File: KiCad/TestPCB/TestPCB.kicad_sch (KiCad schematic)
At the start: 73 parts, among them U1 MC33078, U2 TLC274, U3 MC33078, U4 MC33078, U5 MC33078, U6 TLC274, U7 REF192, U8 DAC5578xPW

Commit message: Schematic re-accommodating
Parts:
- removed JP2, JP3, JP4, JP5, JP6, JP7: Jumper_2_Bridged, symbol Jumper:Jumper_2_Bridged
- removed R12, R13, R14, R15, R16, R17, R2, R3, R4, R5, R6, R7: 10k, symbol Device:R
- removed R22, R23, R24, R25, R26, R27: 1meg, symbol Device:R
- removed R32, R33, R34, R35, R36, R37: 10, symbol Device:R
- removed TP0, TP1, TP2, TP3, TP4, TP5, TP6, TP7: TestPoint, symbol Connector:TestPoint
- removed unit 3 of U2
- removed unit 4 of U2
- removed U5: MC33078, symbol Amplifier_Operational:MC33078
- added JPout_U2a, JPout_U2b, JPout_U3a, JPout_U3b, JPout_U4a, JPout_U4b: Jumper_2_Bridged, symbol Jumper:Jumper_2_Bridged
- added Rain_U5c, Rain_U5d, Rain_U6a, Rain_U6b, Rain_U6c, Rain_U6d: 1meg, symbol Device:R
- added Rbin_U5c, Rbin_U5d, Rbin_U6a, Rbin_U6b, Rbin_U6c, Rbin_U6d: 10, symbol Device:R
- added Rf_U2a, Rf_U2b, Rf_U3a, Rf_U3b, Rf_U4a, Rf_U4b, Rin-_U2a, Rin-_U2b, Rin-_U3a, Rin-_U3b, Rin-_U4a, Rin-_U4b: 10k, symbol Device:R
- added unit 2 of U2
- added unit 1 of U2
- added unit 4 of U5
- added unit 3 of U5
- U3, U4: value MC33078 -> (none)
- U5: renamed from U2; value TLC274 -> (none)
- U6: value TLC274 -> (none)
- gave numbers to parts that had none: 6
- renumbered JP0 to JPout_U1a, JP1 to JPout_U1b, R20 to Rain_U5a, R21 to Rain_U5b, R30 to Rbin_U5a, R31 to Rbin_U5b, R10 to Rf_U1a, R11 to Rf_U1b, R0 to Rin-_U1a, R1 to Rin-_U1b
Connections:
- net GND: now also U8.14 (GND), Rbin_U5c.2, Rbin_U5d.2, Rbin_U6a.2, Rbin_U6b.2, Rbin_U6c.2, Rbin_U6d.2
- net -2V5: now reaches U1.4 (V-)
- net -2V5: now also U2.4 (V-), U3.4 (V-), U4.4 (V-), U5.11 (V-), U6.11 (V-)
- net at U3.1: now also JPout_U3a.1 (A), Rf_U3a.2
- net at U3.2 (-): now also Rf_U3a.1, Rin-_U3a.2
- net at U8.5 (VOUTC): now also U2.3 (+); no longer U3.3 (+)
- net at U3.5 (+): now also U8.11 (VOUTF); no longer U8.12 (VOUTD)
- net at U3.6 (-): now also Rf_U3b.1, Rin-_U3b.2
- net at U3.7: now also JPout_U3b.1 (A), Rf_U3b.2
- net at U4.5 (+): now also U8.10 (VOUTH); no longer U8.11 (VOUTF)
- net at U4.6 (-): now also Rf_U4b.1, Rin-_U4b.2
- net at U4.7: now also JPout_U4b.1 (A), Rf_U4b.2
- net at U4.1: now also JPout_U4a.1 (A), Rf_U4a.2
- net at U4.2 (-): now also Rf_U4a.1, Rin-_U4a.2
- net at U8.6 (VOUTE): now also U3.3 (+); no longer U4.3 (+)
- net at U8.7 (VOUTG): now also U4.3 (+)
- net at U6.3 (+): now also Rain_U6a.2, Rbin_U6a.1
- net at U6.10 (+): now also Rain_U6c.2, Rbin_U6c.1
- net at U6.12 (+): now also Rain_U6d.2, Rbin_U6d.1
- net at U6.5 (+): now also Rain_U6b.2, Rbin_U6b.1
- net at C3.1, Rin-_U1a.1, Rin-_U1b.1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: now also Rin-_U2a.1, Rin-_U2b.1, Rin-_U3a.1, Rin-_U3b.1, Rin-_U4a.1, Rin-_U4b.1
- new net: U2.5 (+), U8.12 (VOUTD)
- new net: Rf_U2b.1, Rin-_U2b.2, U2.6 (-)
- new net: JPout_U2b.1 (A), Rf_U2b.2, U2.7
- new net: JPout_U2a.1 (A), Rf_U2a.2, U2.1
- new net: JPout_U2a.2 (B), Rain_U5c.1
- new net: JPout_U4a.2 (B), Rain_U6c.1
- new net: JPout_U3b.2 (B), Rain_U6b.1
- new net: JPout_U4b.2 (B), Rain_U6d.1
- new net: Rf_U2a.1, Rin-_U2a.2, U2.2 (-)
- new net: JPout_U2b.2 (B), Rain_U5d.1
- new net: Rain_U5d.2, Rbin_U5d.1, U5.12 (+)
- new net: U5.13 (-), U5.14
- new net: Rain_U5c.2, Rbin_U5c.1, U5.10 (+)
- new net: U5.8, U5.9 (-)
- new net: JPout_U3a.2 (B), Rain_U6a.1
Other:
- moved on the sheet: C1, C2, C3, JPout_U1a, JPout_U1b, J_LDAC, J_SCL, J_SDA, J_SYNC, R_SCL, R_SDA, Rain_U5a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

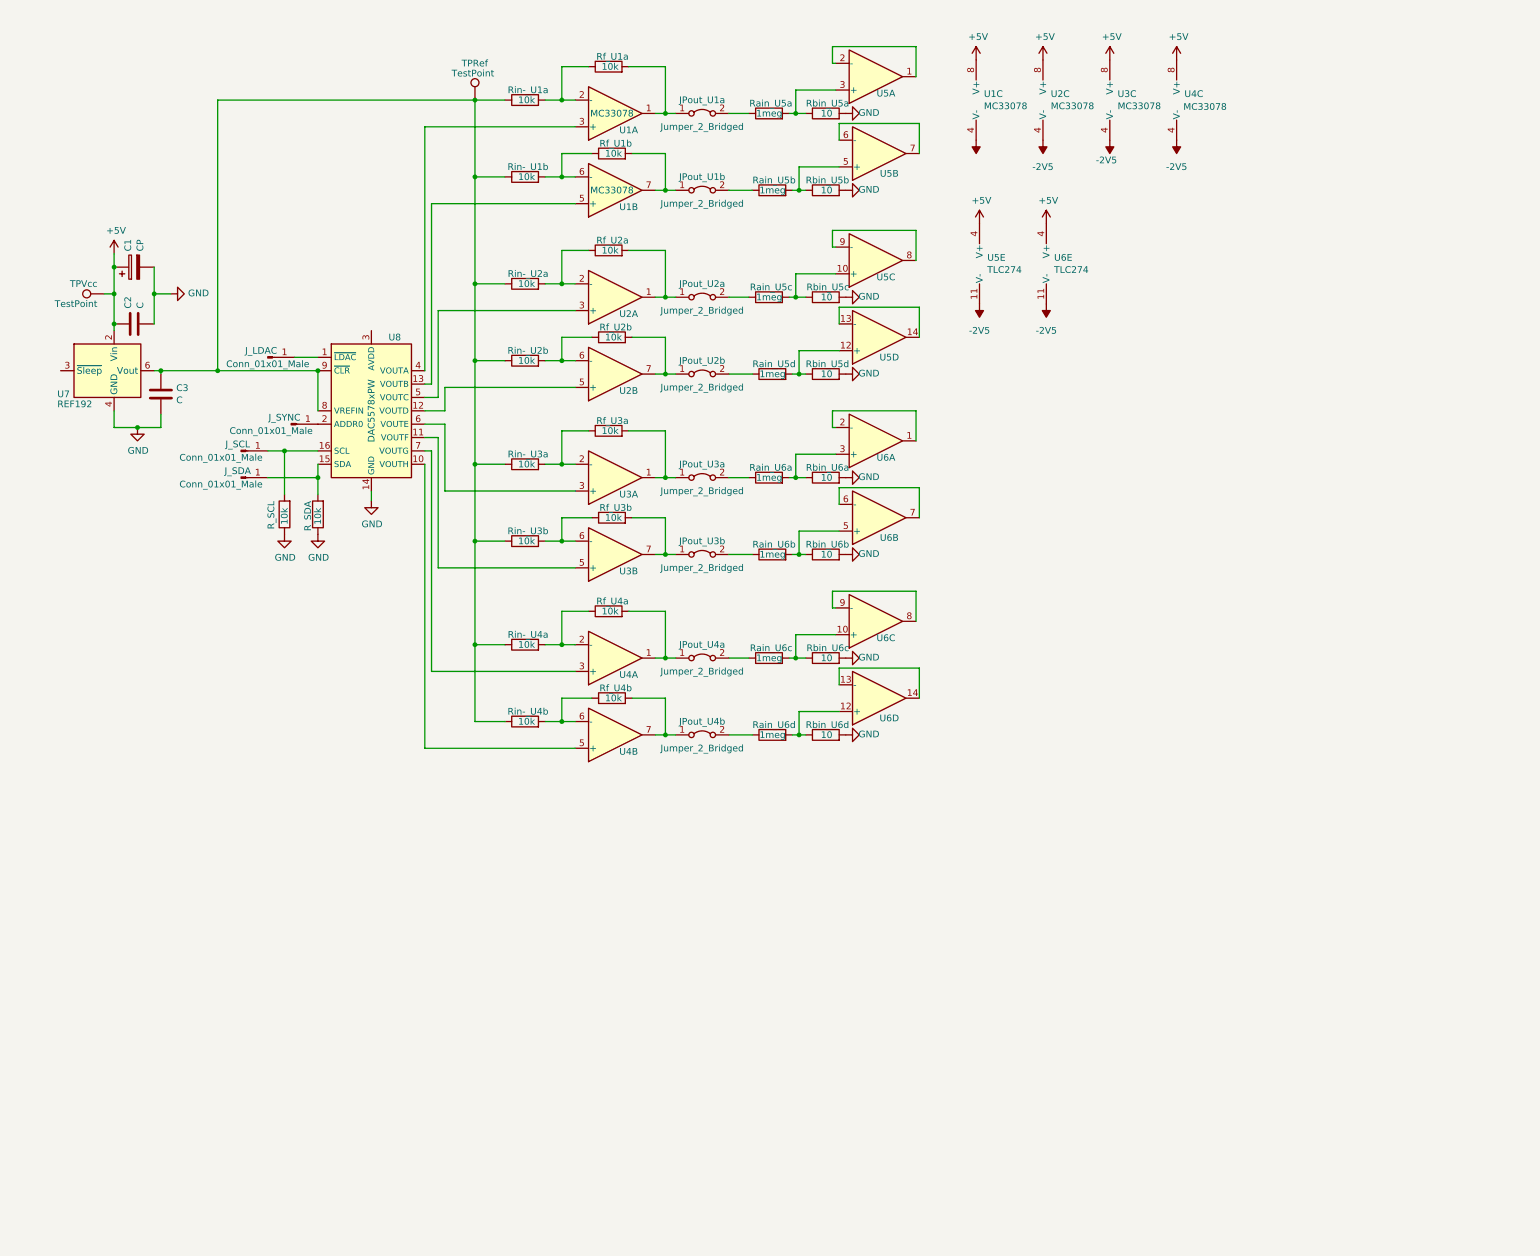
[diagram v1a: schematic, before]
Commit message: component naming and some footprints
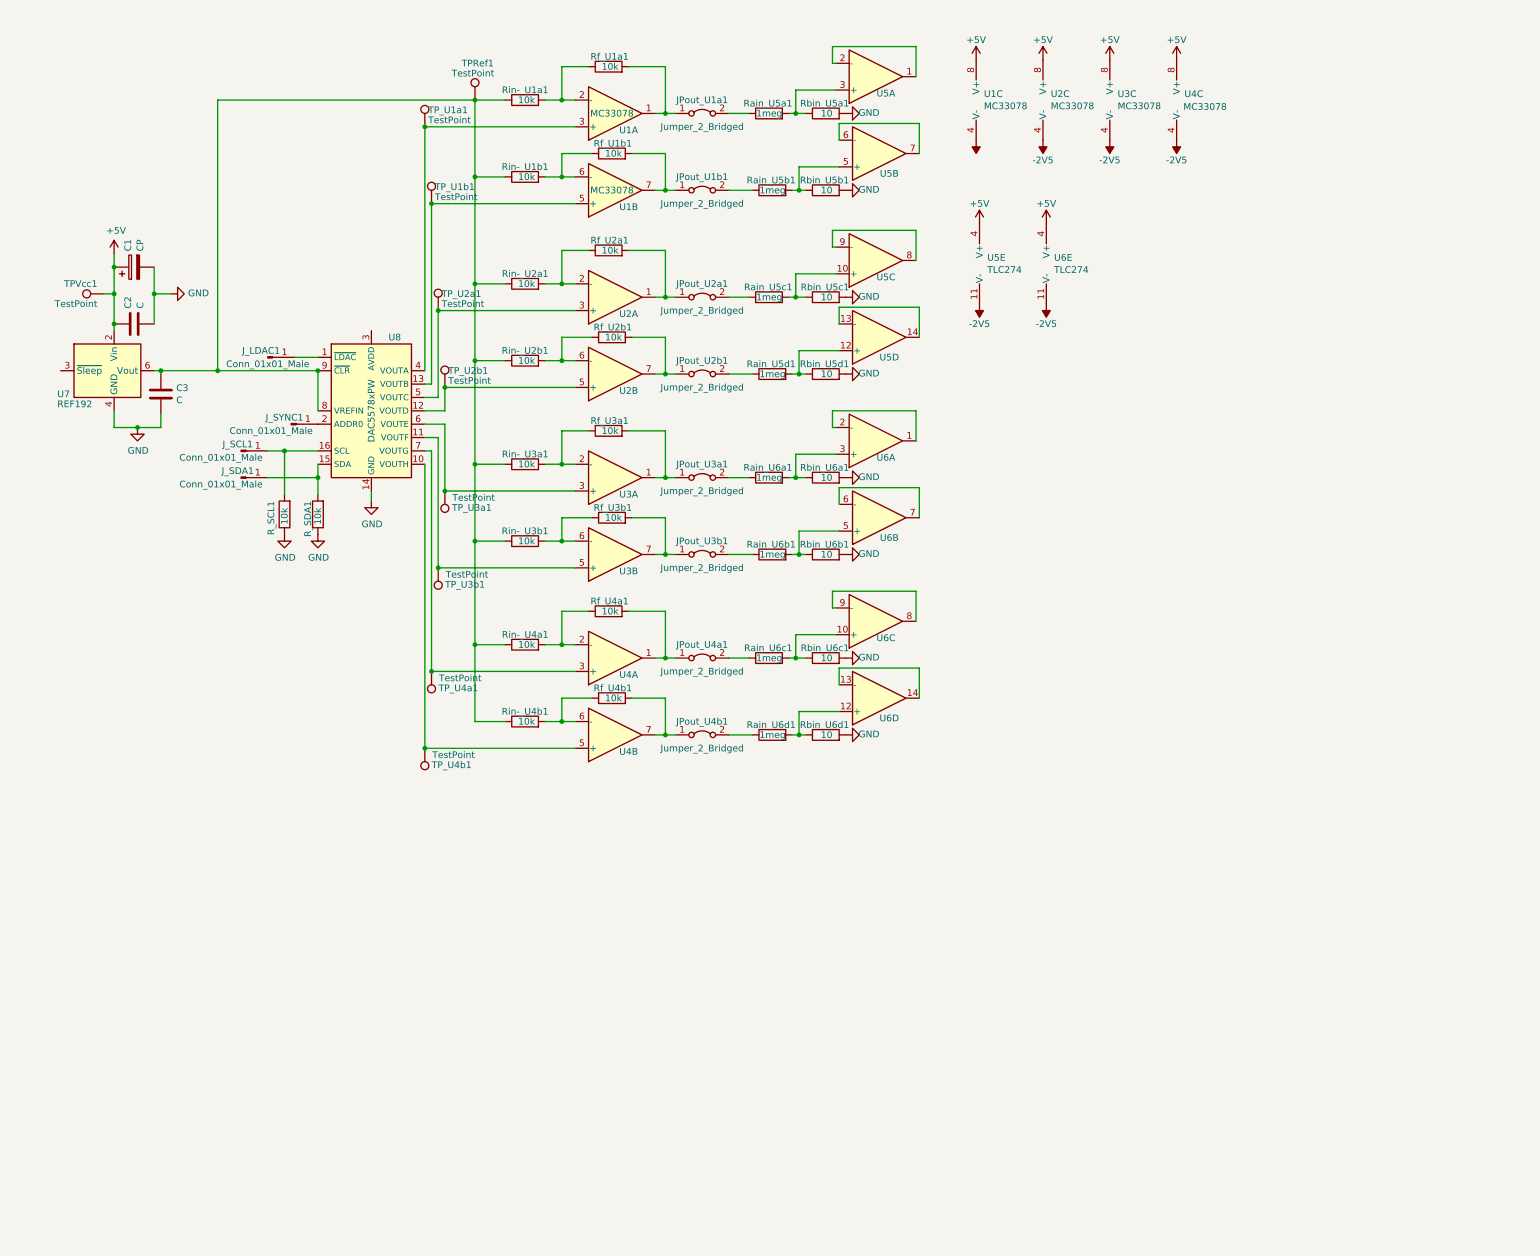
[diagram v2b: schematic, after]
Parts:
- added TP_U1a1, TP_U1b1, TP_U2a1, TP_U2b1, TP_U3a1, TP_U3b1, TP_U4a1, TP_U4b1: TestPoint, symbol Connector:TestPoint
- renumbered JPout_U1a to JPout_U1a1, JPout_U1b to JPout_U1b1, JPout_U2a to JPout_U2a1, JPout_U2b to JPout_U2b1, JPout_U3a to JPout_U3a1, JPout_U3b to JPout_U3b1, JPout_U4a to JPout_U4a1, JPout_U4b to JPout_U4b1, J_LDAC to J_LDAC1, J_SCL to J_SCL1, J_SDA to J_SDA1, J_SYNC to J_SYNC1, R_SCL to R_SCL1, R_SDA to R_SDA1, Rain_U5a to Rain_U5a1, Rain_U5b to Rain_U5b1, Rain_U5c to Rain_U5c1, Rain_U5d to Rain_U5d1, Rain_U6a to Rain_U6a1, Rain_U6b to Rain_U6b1, Rain_U6c to Rain_U6c1, Rain_U6d to Rain_U6d1, Rbin_U5a to Rbin_U5a1, Rbin_U5b to Rbin_U5b1, Rbin_U5c to Rbin_U5c1, Rbin_U5d to Rbin_U5d1, Rbin_U6a to Rbin_U6a1, Rbin_U6b to Rbin_U6b1, Rbin_U6c to Rbin_U6c1, Rbin_U6d to Rbin_U6d1, Rf_U1a to Rf_U1a1, Rf_U1b to Rf_U1b1, Rf_U2a to Rf_U2a1, Rf_U2b to Rf_U2b1, Rf_U3a to Rf_U3a1, Rf_U3b to Rf_U3b1, Rf_U4a to Rf_U4a1, Rf_U4b to Rf_U4b1, Rin-_U1a to Rin-_U1a1, Rin-_U1b to Rin-_U1b1, Rin-_U2a to Rin-_U2a1, Rin-_U2b to Rin-_U2b1, Rin-_U3a to Rin-_U3a1, Rin-_U3b to Rin-_U3b1, Rin-_U4a to Rin-_U4a1, Rin-_U4b to Rin-_U4b1, TPRef to TPRef1, TPVcc to TPVcc1
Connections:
- net at U1.3 (+), U8.4 (VOUTA): now also TP_U1a1.1
- net at U1.5 (+), U8.13 (VOUTB): now also TP_U1b1.1
- net at U4.5 (+), U8.10 (VOUTH): now also TP_U4b1.1
- net at U3.5 (+), U8.11 (VOUTF): now also TP_U3b1.1
- net at U2.5 (+), U8.12 (VOUTD): now also TP_U2b1.1
- net at U2.3 (+), U8.5 (VOUTC): now also TP_U2a1.1
- net at U3.3 (+), U8.6 (VOUTE): now also TP_U3a1.1
- net at U4.3 (+), U8.7 (VOUTG): now also TP_U4a1.1

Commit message: schematic done, mock footprints assigned
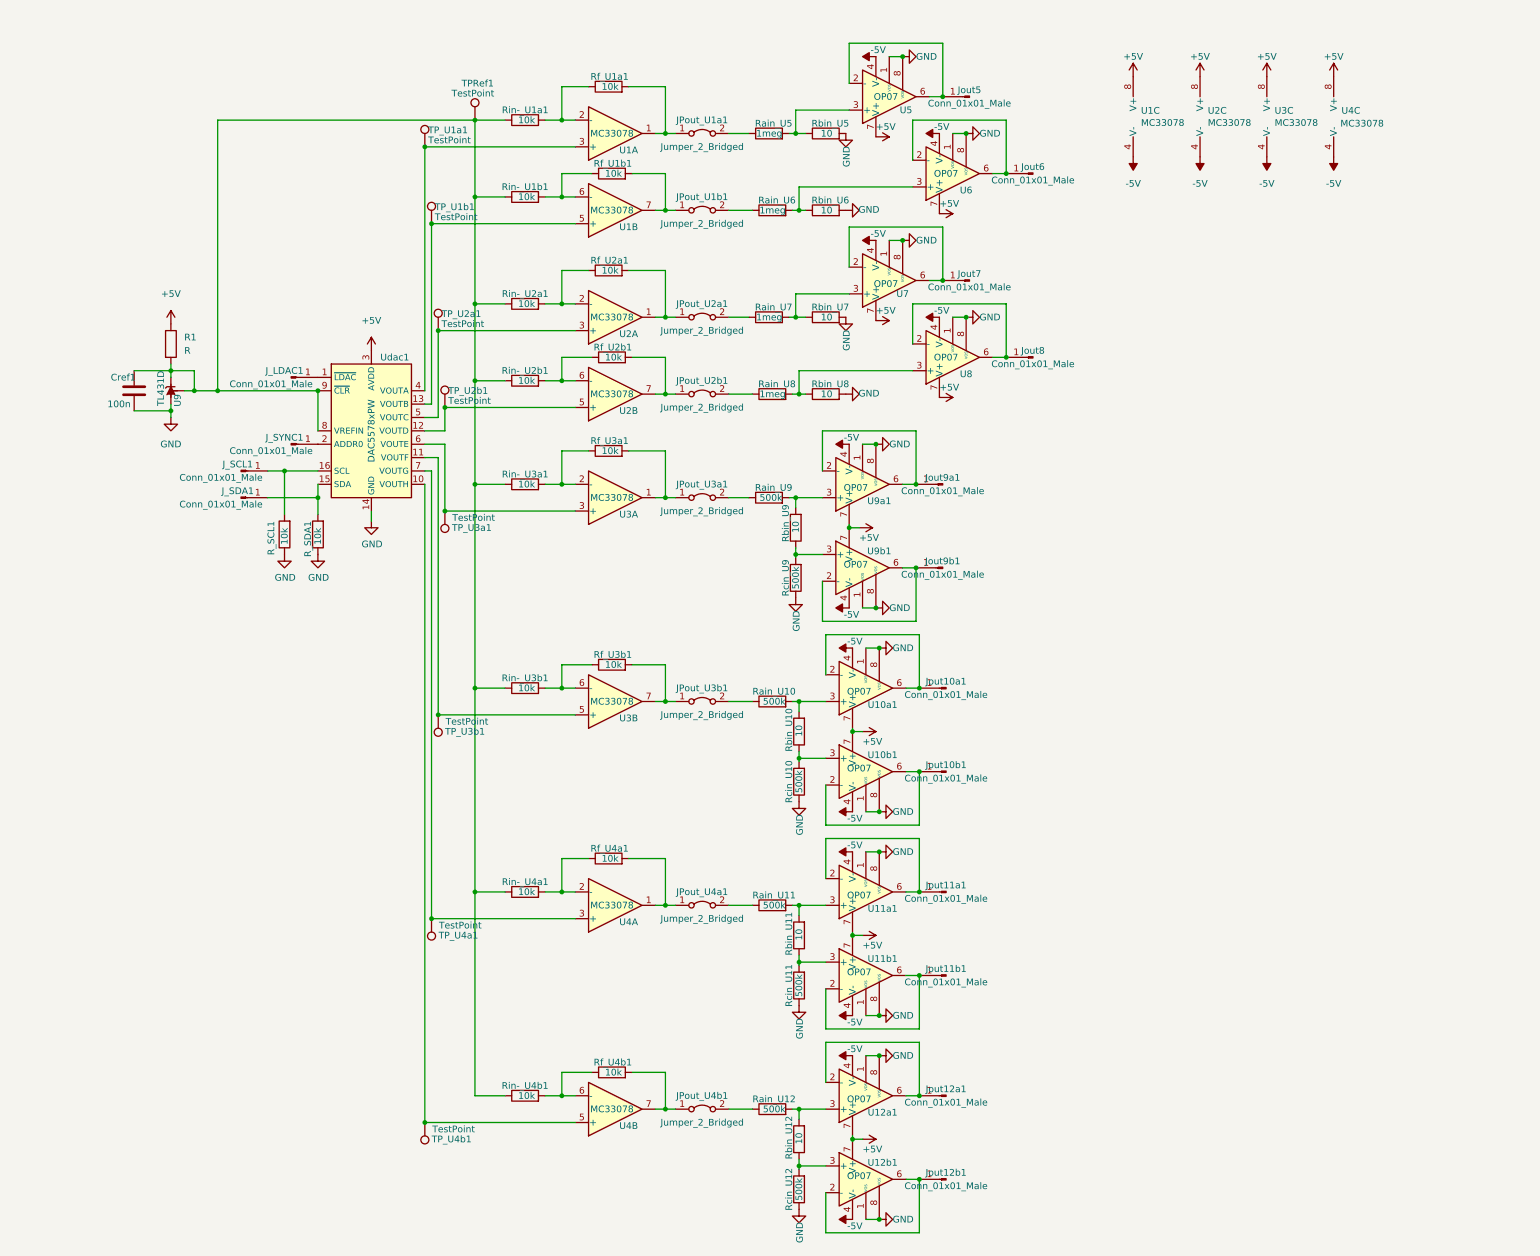
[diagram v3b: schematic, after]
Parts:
- removed C1: CP, symbol TestPCB-rescue:CP-Device
- removed C2, C3: C, symbol Device:C
- removed Rain_U6b1, Rain_U6c1, Rain_U6d1: 1meg, symbol Device:R
- removed Rbin_U6b1, Rbin_U6c1, Rbin_U6d1: 10, symbol Device:R
- removed TPVcc1: TestPoint, symbol Connector:TestPoint
- removed U5: (no value), symbol Amplifier_Operational:TLC274
- removed U6: TLC274, symbol Amplifier_Operational:TLC274
- removed U7: REF192, symbol Reference_Voltage:REF192
- added Cref1: 100n, Capacitor_THT:C_Disc_D5.0mm_W2.5mm_P5.00mm, symbol Device:C
- added Jout10a1, Jout10b1, Jout11a1, Jout11b1, Jout12a1, Jout12b1, Jout5, Jout6, Jout7, Jout8, Jout9a1, Jout9b1: Conn_01x01_Male, Connector_PinHeader_2.54mm:PinHeader_1x01_P2.54mm_Vertical, symbol Connector:Conn_01x01_Male
- added R1: R, Resistor_THT:R_Axial_DIN0207_L6.3mm_D2.5mm_P10.16mm_Horizontal, symbol Device:R
- added Rain_U10, Rain_U11, Rain_U12, Rcin_U10, Rcin_U11, Rcin_U12, Rcin_U9: 500k, Resistor_SMD:R_2010_5025Metric_Pad1.40x2.65mm_HandSolder, symbol Device:R
- added Rbin_U10, Rbin_U11, Rbin_U12: 10, Resistor_SMD:R_2010_5025Metric_Pad1.40x2.65mm_HandSolder, symbol Device:R
- added U10a1, U10b1, U11a1, U11b1, U12a1, U12b1, U5, U6, U7, U8, U9a1, U9b1: OP07, Package_SO:SOIC-8_3.9x4.9mm_P1.27mm, symbol Amplifier_Operational:OP07
- added U9: TL431D, Package_SO:SOIC-8_3.9x4.9mm_P1.27mm, symbol Reference_Voltage:TL431D
- JPout_U1a1, JPout_U1b1, JPout_U2a1, JPout_U2b1, JPout_U3a1, JPout_U3b1, JPout_U4a1, JPout_U4b1: footprint (none) -> Connector_PinHeader_2.54mm:PinHeader_1x02_P2.54mm_Vertical
- J_LDAC1, J_SCL1, J_SDA1, J_SYNC1: footprint (none) -> Connector_PinHeader_2.54mm:PinHeader_1x01_P2.54mm_Vertical
- R_SCL1, R_SDA1, Rf_U1a1, Rf_U1b1, Rf_U2a1, Rf_U2b1, Rf_U3a1, Rf_U3b1, Rf_U4a1, Rf_U4b1, Rin-_U1a1, Rin-_U1b1, Rin-_U2a1, Rin-_U2b1, Rin-_U3a1, Rin-_U3b1, Rin-_U4a1, Rin-_U4b1: footprint (none) -> Resistor_THT:R_Axial_DIN0207_L6.3mm_D2.5mm_P10.16mm_Horizontal
- Rain_U5: renamed from Rain_U5a1; footprint (none) -> Resistor_SMD:R_2010_5025Metric_Pad1.40x2.65mm_HandSolder
- Rain_U6: renamed from Rain_U5b1; footprint (none) -> Resistor_SMD:R_2010_5025Metric_Pad1.40x2.65mm_HandSolder
- Rain_U7: renamed from Rain_U5c1; footprint (none) -> Resistor_SMD:R_2010_5025Metric_Pad1.40x2.65mm_HandSolder
- Rain_U8: renamed from Rain_U5d1; footprint (none) -> Resistor_SMD:R_2010_5025Metric_Pad1.40x2.65mm_HandSolder
- Rain_U9: renamed from Rain_U6a1; value 1meg -> 500k; footprint (none) -> Resistor_SMD:R_2010_5025Metric_Pad1.40x2.65mm_HandSolder
- Rbin_U5: renamed from Rbin_U5a1; footprint (none) -> Resistor_SMD:R_2010_5025Metric_Pad1.40x2.65mm_HandSolder
- Rbin_U6: renamed from Rbin_U5b1; footprint (none) -> Resistor_SMD:R_2010_5025Metric_Pad1.40x2.65mm_HandSolder
- Rbin_U7: renamed from Rbin_U5c1; footprint (none) -> Resistor_SMD:R_2010_5025Metric_Pad1.40x2.65mm_HandSolder
- Rbin_U8: renamed from Rbin_U5d1; footprint (none) -> Resistor_SMD:R_2010_5025Metric_Pad1.40x2.65mm_HandSolder
- Rbin_U9: renamed from Rbin_U6a1; footprint (none) -> Resistor_SMD:R_2010_5025Metric_Pad1.40x2.65mm_HandSolder
- TPRef1, TP_U1a1, TP_U1b1, TP_U2a1, TP_U2b1, TP_U3a1, TP_U3b1, TP_U4a1, TP_U4b1: footprint (none) -> TestPoint:TestPoint_Pad_4.0x4.0mm
- U1, U2, U3, U4: footprint (none) -> Package_DIP:DIP-8_W7.62mm_Socket_LongPads
- U2, U3, U4: value (none) -> MC33078; footprint (none) -> Package_DIP:DIP-8_W7.62mm_Socket_LongPads
- renumbered U8 to Udac1
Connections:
- net +5V: now also Udac1.3 (AVDD), R1.1, U10a1.7 (V+), U10b1.7 (V+), U11a1.7 (V+), U11b1.7 (V+), U12a1.7 (V+), U12b1.7 (V+), U5.7 (V+), U6.7 (V+), U7.7 (V+), U8.7 (V+), U9a1.7 (V+), U9b1.7 (V+)
- net GND: now also Cref1.2, Rcin_U10.1, Rcin_U11.1, Rcin_U12.1, Rcin_U9.1, U10a1.1 (VOS), U10a1.8 (VOS), U10b1.1 (VOS), U10b1.8 (VOS), U11a1.1 (VOS), U11a1.8 (VOS), U11b1.1 (VOS), U11b1.8 (VOS), U12a1.1 (VOS), U12a1.8 (VOS), U12b1.1 (VOS), U12b1.8 (VOS), U5.1 (VOS), U5.8 (VOS), U6.1 (VOS), U6.8 (VOS), U7.1 (VOS), U7.8 (VOS), U8.1 (VOS), U8.8 (VOS), U9.2 (A), U9.3 (A), U9.6 (A), U9.7 (A), U9a1.1 (VOS), U9a1.8 (VOS), U9b1.1 (VOS), U9b1.8 (VOS); no longer Rbin_U9.2
- net at Rain_U5.2, Rbin_U5.1: now also U5.3 (+)
- net at Rain_U6.2, Rbin_U6.1: now also U6.3 (+)
- net at Rin-_U1a1.1, Rin-_U1b1.1, Rin-_U2a1.1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: now also Cref1.1, R1.2, U9.1 (K), U9.8 (REF)
- net at JPout_U4a1.2 (B): now also Rain_U11.1
- net at JPout_U3b1.2 (B): now also Rain_U10.1
- net at JPout_U4b1.2 (B): now also Rain_U12.1
- net at Rbin_U9.1: now also Rcin_U9.2, U9b1.3 (+); no longer Rain_U9.2
- net at Rain_U8.2, Rbin_U8.1: now also U8.3 (+)
- net at Rain_U7.2, Rbin_U7.1: now also U7.3 (+)
- net -2V5 renamed -5V
- net -5V: now also U10a1.4 (V-), U10b1.4 (V-), U11a1.4 (V-), U11b1.4 (V-), U12a1.4 (V-), U12b1.4 (V-), U5.4 (V-), U6.4 (V-), U7.4 (V-), U8.4 (V-), U9a1.4 (V-), U9b1.4 (V-)
- new net: Jout8.1 (Pin_1), U8.2 (-), U8.6
- new net: Jout10a1.1 (Pin_1), U10a1.2 (-), U10a1.6
- new net: Rain_U10.2, Rbin_U10.2, U10a1.3 (+)
- new net: Jout9a1.1 (Pin_1), U9a1.2 (-), U9a1.6
- new net: Jout9b1.1 (Pin_1), U9b1.2 (-), U9b1.6
- new net: Jout11a1.1 (Pin_1), U11a1.2 (-), U11a1.6
- new net: Jout10b1.1 (Pin_1), U10b1.2 (-), U10b1.6
- new net: Jout6.1 (Pin_1), U6.2 (-), U6.6
- new net: Rbin_U10.1, Rcin_U10.2, U10b1.3 (+)
- new net: Jout12b1.1 (Pin_1), U12b1.2 (-), U12b1.6
- new net: Rbin_U11.1, Rcin_U11.2, U11b1.3 (+)
- new net: Rain_U9.2, Rbin_U9.2, U9a1.3 (+)
- new net: Jout11b1.1 (Pin_1), U11b1.2 (-), U11b1.6
- new net: Rbin_U12.1, Rcin_U12.2, U12b1.3 (+)
- new net: Jout7.1 (Pin_1), U7.2 (-), U7.6
- new net: Rain_U11.2, Rbin_U11.2, U11a1.3 (+)
- new net: Jout12a1.1 (Pin_1), U12a1.2 (-), U12a1.6
- new net: Rain_U12.2, Rbin_U12.2, U12a1.3 (+)
- new net: Jout5.1 (Pin_1), U5.2 (-), U5.6
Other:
- moved on the sheet: JPout_U1a1, JPout_U1b1, JPout_U2a1, JPout_U2b1, JPout_U3a1, JPout_U3b1, JPout_U4a1, JPout_U4b1, J_LDAC1, J_SCL1, J_SDA1, J_SYNC1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

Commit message: PCB progress, our outputs done
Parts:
- removed TPRef1: TestPoint, TestPoint:TestPoint_Pad_4.0x4.0mm, symbol Connector:TestPoint
- added TPRef1: (no value), symbol Connector:Conn_01x01_Male
- U10a1, U10b1, U11a1, U11b1, U12a1, U12b1, U5, U6, U7, U8, U9a1, U9b1: footprint Package_SO:SOIC-8_3.9x4.9mm_P1.27mm -> (none)
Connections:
- net at TP_U1a1.1, U1.3 (+): now also Udac1.13 (VOUTB); no longer Udac1.4 (VOUTA)
- net at TP_U1b1.1, U1.5 (+): now also Udac1.12 (VOUTD); no longer Udac1.13 (VOUTB)
- net +2V5: now reaches Cref1.1, R1.2, Rin-_U1a1.1, Rin-_U1b1.1, Rin-_U2a1.1, Rin-_U2b1.1, Rin-_U3a1.1, Rin-_U3b1.1, Rin-_U4a1.1, Rin-_U4b1.1, U9.1 (K), U9.8 (REF), Udac1.8 (VREFIN), Udac1.9 (~{CLR})
- net +2V5: now also TPRef1.1 (Pin_1)
- net at TP_U4b1.1, U4.5 (+): now also Udac1.7 (VOUTG); no longer Udac1.10 (VOUTH)
- net at TP_U3b1.1, U3.5 (+): now also Udac1.5 (VOUTC); no longer Udac1.11 (VOUTF)
- net at TP_U2b1.1, U2.5 (+): now also Udac1.10 (VOUTH); no longer Udac1.12 (VOUTD)
- net at TP_U2a1.1, U2.3 (+): now also Udac1.11 (VOUTF); no longer Udac1.5 (VOUTC)
- net at TP_U3a1.1, U3.3 (+): now also Udac1.4 (VOUTA); no longer Udac1.6 (VOUTE)
- net at TP_U4a1.1, U4.3 (+): now also Udac1.6 (VOUTE); no longer Udac1.7 (VOUTG)
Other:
- moved on the sheet: TP_U1a1, TP_U1b1, TP_U2a1, TP_U2b1, TP_U3a1, TP_U4a1, TP_U4b1
